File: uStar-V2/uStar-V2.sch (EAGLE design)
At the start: 47 parts, among them IC1 INA138, IC2 SN74HC4066PWRTSSOP, IC3 SN74HC4066PWRTSSOP, IC4 SN74HC4066PWRTSSOP, IC5 SN74HC4066PWRTSSOP, M1 Mount, M2 Mount, U2 SD_CARD, X2 BU-SMA-H, X3 BU-SMA-H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

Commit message: added the 3D parts to the library added cost and hours to the BOM
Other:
- note added: "Feed 5V to pin Vin/Gnd on PWR2"
- note added: "Ground Station Assembly Variant"
- note added: "Jumper BoardVCC to Radio_VCC_3_3"
- note added: "Jumper IC2 and IC4 straight through"
- note added: "Jumper for ground station variant only"

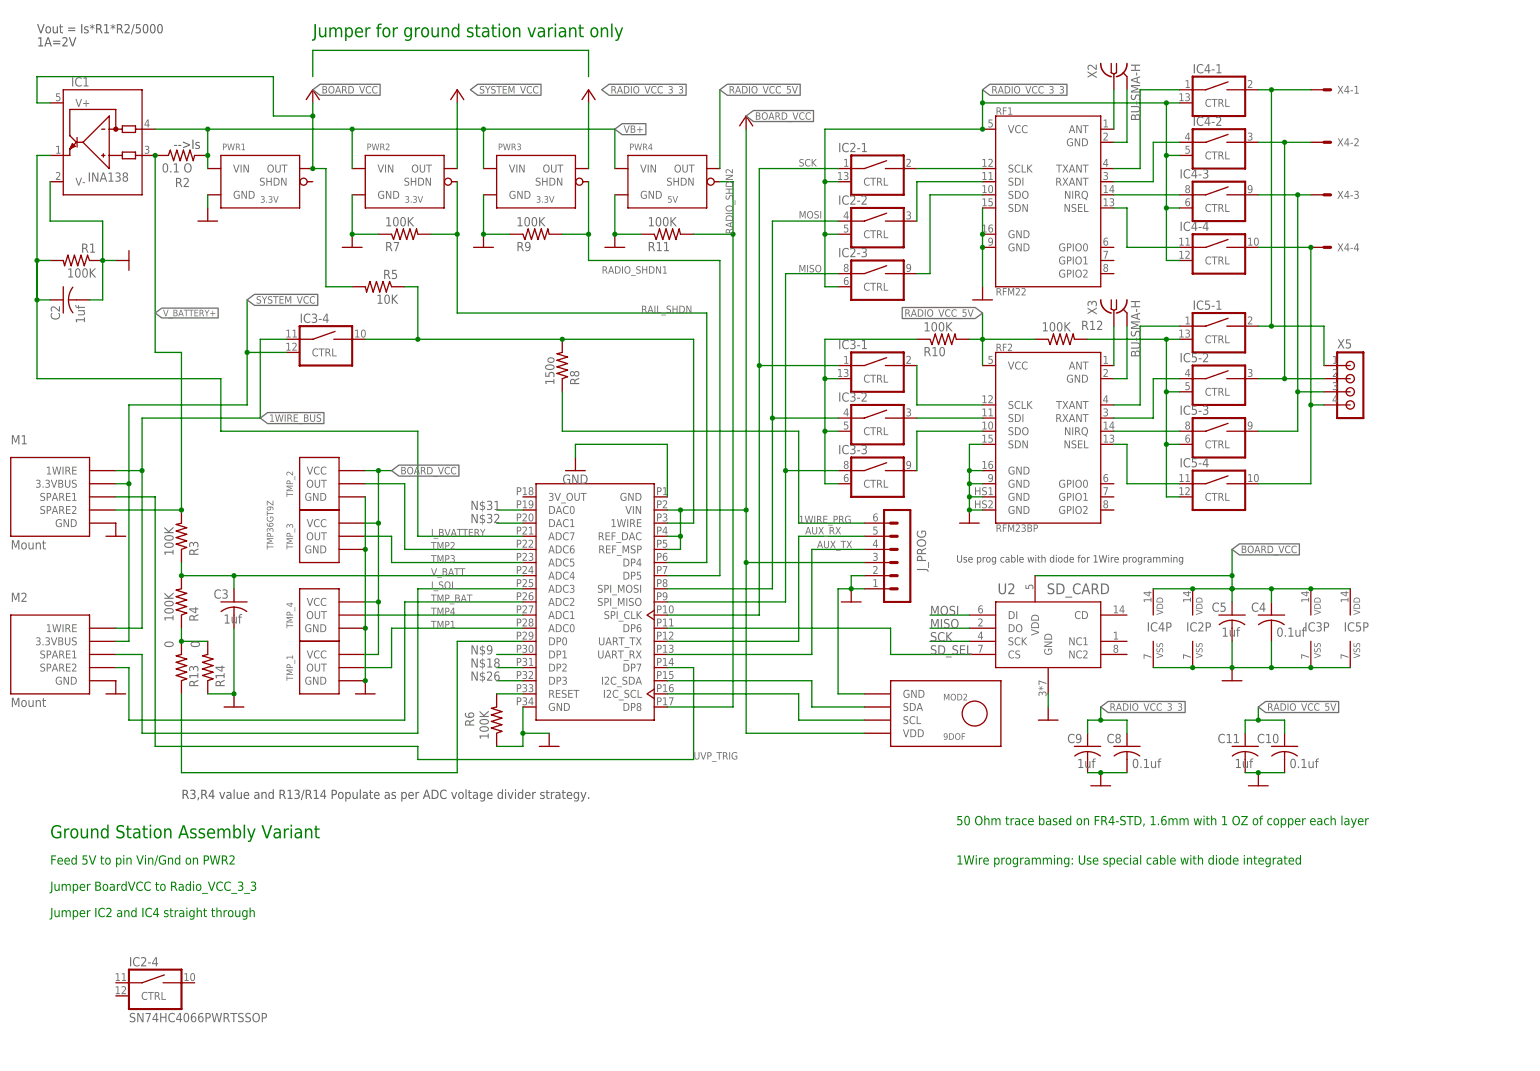
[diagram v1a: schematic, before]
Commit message: 
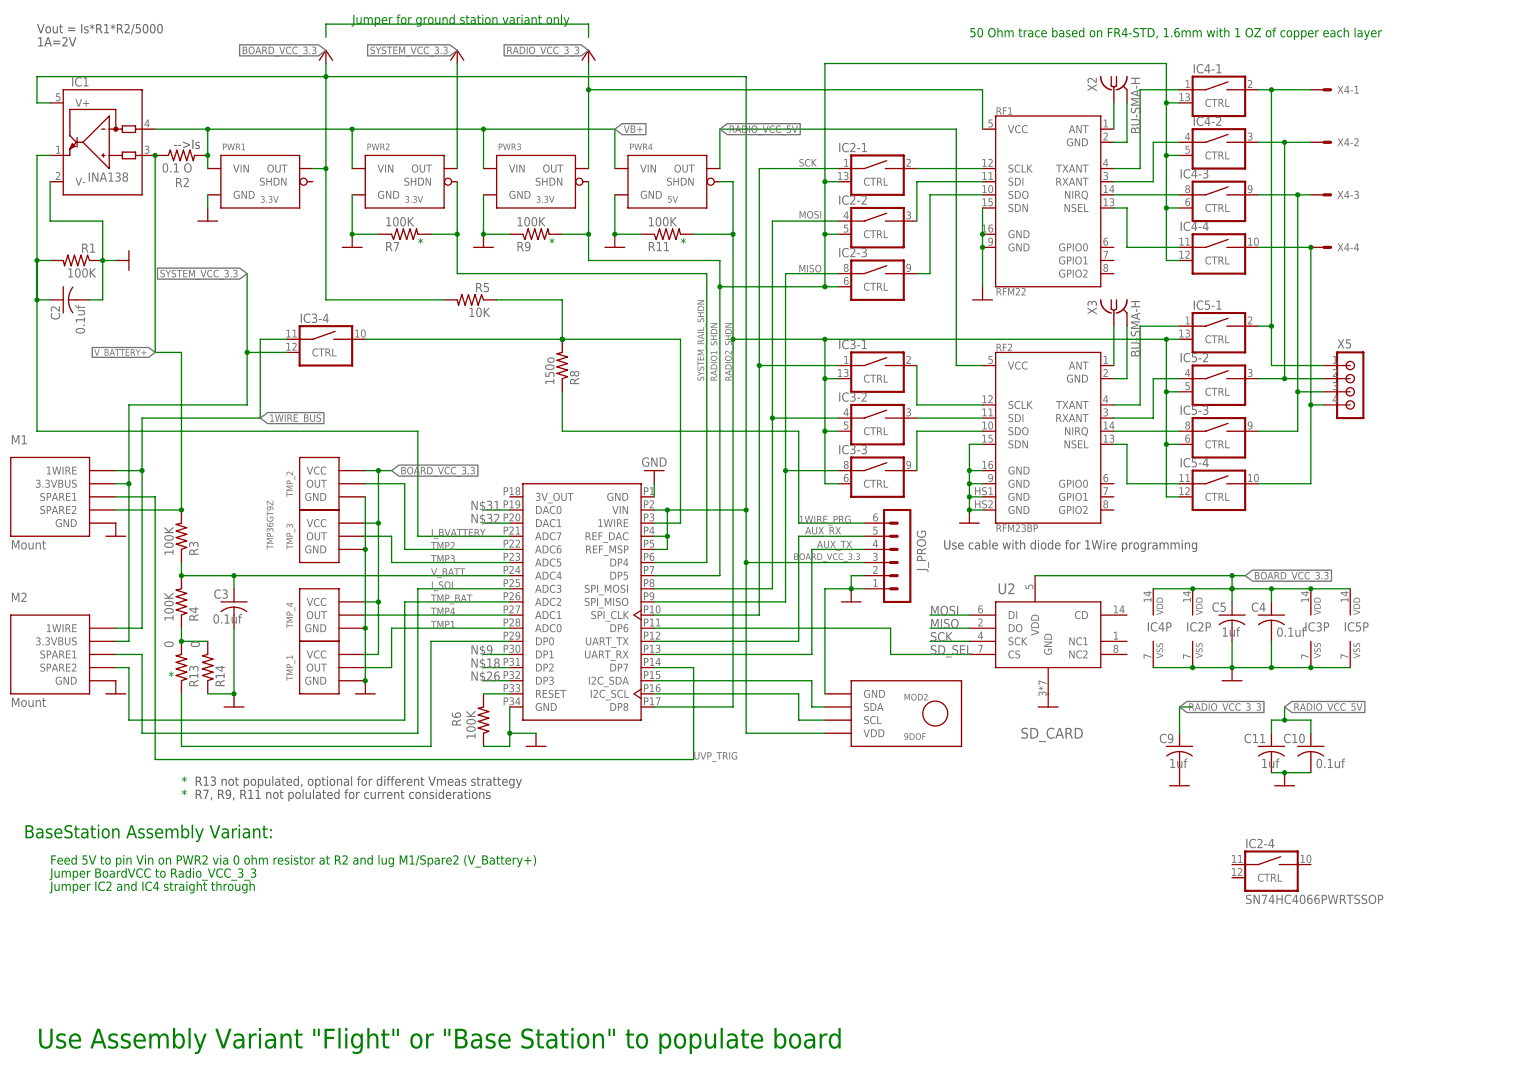
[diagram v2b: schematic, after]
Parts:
- removed C8: 0.1uf, rcl:C-USC0805
- removed R10, R12: 100K, rcl:R-US_R0805
- C2, C3: value 1uf -> 0.1uf
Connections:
- net BOARD_VCC renamed BOARD_VCC_3.3
- net RAIL_SHDN renamed SYSTEM_RAIL_SHDN
- net SYSTEM_VCC renamed SYSTEM_VCC_3.3
- removed net N$4: IC3-1.CTRL, IC3-2.CTRL, IC3-3.CTRL, R10.1
- removed net N$8: IC5-1.CTRL, IC5-2.CTRL, IC5-3.CTRL, IC5-4.CTRL, R12.2
- removed net RADIO_SHDN1: MOD1.DP5, PWR3.SHDN, R9.2
- removed net RADIO_SHDN2: MOD1.DP8, PWR4.SHDN, R11.2
- new net RADIO1_SHDN: IC2-1.CTRL, IC2-2.CTRL, IC2-3.CTRL, IC4-1.CTRL, IC4-2.CTRL, IC4-3.CTRL, IC4-4.CTRL, MOD1.DP5, PWR3.SHDN, R9.2
- new net RADIO2_SHDN: IC3-1.CTRL, IC3-2.CTRL, IC3-3.CTRL, IC5-1.CTRL, IC5-2.CTRL, IC5-3.CTRL, IC5-4.CTRL, MOD1.DP8, PWR4.SHDN, R11.2
- net GND: no longer C8.2
- net RADIO_VCC_3_3: no longer C8.1, IC2-1.CTRL, IC2-2.CTRL, IC2-3.CTRL, IC4-1.CTRL, IC4-2.CTRL, IC4-3.CTRL, IC4-4.CTRL
- net RADIO_VCC_5V: no longer R10.2, R12.1
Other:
- note added: "*"
- note added: "BaseStation Assembly Variant:"
- note added: "Feed 5V to pin Vin on PWR2 via 0 ohm resistor at R2 and lug M1/Spare2 (V_Battery+)"
- note added: "R13 not populated, optional for different Vmeas strattegy"
- note added: "R7, R9, R11 not polulated for current considerations"
- note added: "Use Assembly Variant "Flight" or "Base Station" to populate board"
- note added: "Use cable with diode for 1Wire programming"
- note removed: "1Wire programming: Use special cable with diode integrated"
- note removed: "Feed 5V to pin Vin/Gnd on PWR2"
- note removed: "Ground Station Assembly Variant"
- note removed: "R3,R4 value and R13/R14 Populate as per ADC voltage divider strategy."
- note removed: "Use prog cable with diode for 1Wire programming"
- moved on the sheet: C10, C11, C9, IC2-4, MOD2, R5, R6, X2

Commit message: Changed solder stop mask to fully cover vias to protect from short with RFM23bp. Changed brd rev label to 2.1b to reflect above. Added R9 and R11 back into the flight build - Inadvertently removed when adding the GND station build option. Added wiring schematic for FTDI cable and connector to sch Added ECO sheet to sch change or R6 to Capacitor 0.1uf -- Reset Issue resolve.
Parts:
- added D1: 1N4148DO35-7, diode:1N4148DO35-7
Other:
- note added: "1 Wire /FTDI programming interface:"
- note added: "12/08/21 Affecting PCB Revision 2.1 and 2.1b,Schematic Revision 2.0"
- note added: "12/13/21 Affecting PCB Revision 2.1 and 2.1b,Schematic Revision 2.0"
- note added: "2/25/21 Affecting all builds with radio RFM23bp"
- note added: "Black,GND"
- note added: "FTDI"
- note added: "For BaseStation Jumper IC2: 1-2,3-4,8-9 and IC4 1-2,3-4,8-9,10-11,"
- note added: "J-prog Pin 3 (+3.3V)"
- note added: "J-prog Pin 6 (1 Wire Prog)"
- note added: "J-prog Pin1 (GND)"
- note added: "Jumper for base station variant only"
- note added: "List of Engineering Change Orders (ECO)"
- note added: "Orange, FTDI TX"
- note added: "Place a layer of Kapton tape underneath the big radio where the heatsink pad is located to guard against an eventual short circuit to underlaying traces. V2.1b artwork has covered vias and tape is merely a safety precautoion."
- note added: "R6 : Remove and replace with 805/ 0.1uF ceramic capacitor. Guards against a inadvertant reset condition in an noisy EMF enwironment"
- note added: "R6 changed to 0.1uF capacitor instead of 100k resistor"
- note added: "R7 not polulated for current considerations"
- note added: "R9, R11: Add 805/R10K resistor on empty pads for R9 , R11. Affects the startup sequence of radio power and prevents potential sporadic transmission during uP bootup sequence."
- note added: "Red +3.3V"
- note added: "Yellow, FTDI RX"
- note removed: "Jumper for ground station variant only"
- note removed: "R7, R9, R11 not polulated for current considerations"
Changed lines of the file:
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@@
 <layer number="59" name="tCarbon" color="7" fill="1" visible="no" active="no"/>
 <layer number="60" name="bCarbon" color="7" fill="1" visible="no" active="no"/>
-<layer number="88" name="SimResults" color="9" fill="1" visible="no" active="yes"/>
+<layer number="88" name="SimResults" color="9" fill="1" visible="yes" active="yes"/>
 <layer number="89" name="SimProbes" color="9" fill="1" visible="no" active="yes"/>
 <layer number="90" name="Modules" color="5" fill="1" visible="no" active="yes"/>
@@
 <variantdefs>
 <variantdef name="BaseSation"/>
-<variantdef name="Flight"/>
+<variantdef name="Flight" current="yes"/>
 </variantdefs>
 <classes>
@@
 <attribute name="DIGIKEY" value="2019-RK73H2ATTD1003FCT-ND"/>
 <variant name="BaseSation" populate="no"/>
-<variant name="Flight" populate="no"/>
 </part>
 <part name="R6" library="rcl" library_urn="urn:adsk.eagle:library:334" deviceset="R-US_" device="R0805" package3d_urn="urn:adsk.eagle:package:23553/2" value="100K">
 <attribute name="DIGIKEY" value="2019-RK73H2ATTD1003FCT-ND"/>
+<variant name="BaseSation" populate="no"/>
+<variant name="Flight" populate="no"/>
 </part>
 <part name="X4" library="newUstar" deviceset="?M04B-SRSS-TB" device="S" package3d_urn="urn:adsk.eagle:package:25263025/2">
@@
 <attribute name="DIGIKEY" value="2019-RK73H2ATTD1003FCT-ND"/>
 <variant name="BaseSation" populate="no"/>
-<variant name="Flight" populate="no"/>
 </part>
 <part name="IC4" library="newUstar" deviceset="SN74HC4066PWR" device="TSSOP" package3d_urn="urn:adsk.eagle:package:25264417/2">
@@
 <variant name="BaseSation" populate="no"/>
 </part>
+<part name="D1" library="diode" library_urn="urn:adsk.eagle:library:210" deviceset="1N4148" device="DO35-7" package3d_urn="urn:adsk.eagle:package:43339/2"/>
 </parts>
 <sheets>
@@
 <text x="-93.98" y="78.74" size="1.778" layer="91">Jumper IC2 and IC4 straight through</text>
 <text x="-93.98" y="83.82" size="1.778" layer="91">Feed 5V to pin Vin on PWR2 via 0 ohm resistor at R2 and lug M1/Spare2 (V_Battery+)</text>
-<text x="-99.06" y="88.9" size="2.54" layer="91">BaseStation Assembly Variant:</text>
-<text x="-35.56" y="246.38" size="1.778" layer="91">Jumper for ground station variant only</text>
+<text x="-93.98" y="88.9" size="2.54" layer="91">BaseStation Assembly Variant:</text>
+<text x="-35.56" y="246.38" size="1.778" layer="97">Jumper for base station variant only</text>
 <text x="-71.12" y="119.38" size="1.778" layer="91">*</text>
 <text x="-68.58" y="99.06" size="1.778" layer="91">*</text>
@@
 <text x="27.94" y="203.2" size="1.778" layer="91">*</text>
 <text x="-68.58" y="96.52" size="1.778" layer="91">*</text>
-<text x="-66.04" y="96.52" size="1.778" layer="97">R7, R9, R11 not polulated for current considerations</text>
+<text x="-66.04" y="96.52" size="1.778" layer="97">R7 not polulated for current considerations</text>
+<text x="84.328" y="240.03" size="1.778" layer="97">For BaseStation  Jumper IC2: 1-2,3-4,8-9 and IC4 1-2,3-4,8-9,10-11,</text>
+<text x="-91.44" y="71.12" size="2.54" layer="96">1 Wire /FTDI  programming interface:</text>
+<wire x1="-76.2" y1="68.58" x2="-38.1" y2="68.58" width="0.1524" layer="96"/>
+<wire x1="-78.74" y1="66.04" x2="-43.18" y2="66.04" width="0.1524" layer="96"/>
+<wire x1="-43.18" y1="66.04" x2="-38.1" y2="66.04" width="0.1524" layer="96"/>
+<wire x1="-76.2" y1="63.5" x2="-50.8" y2="63.5" width="0.1524" layer="96"/>
+<wire x1="-76.2" y1="60.96" x2="-38.1" y2="60.96" width="0.1524" layer="96"/>
+<polygon width="0.1524" layer="96">
+<vertex x="-91.44" y="68.58"/>
+<vertex x="-76.2" y="68.58"/>
+<vertex x="-76.2" y="60.96"/>
+<vertex x="-91.44" y="60.96"/>
+</polygon>
+<polygon width="0.1524" layer="96">
+<vertex x="-91.694" y="67.564"/>
+<vertex x="-91.694" y="61.976"/>
+<vertex x="-97.536" y="61.976"/>
+<vertex x="-97.536" y="67.564"/>
+</polygon>
+<text x="-88.9" y="63.5" size="2.54" layer="88">FTDI</text>
+<text x="-71.12" y="68.834" size="1.016" layer="94">Red +3.3V</text>
+<text x="-71.12" y="66.548" size="1.016" layer="94">Yellow, FTDI RX</text>
+<text x="-71.374" y="64.008" size="1.016" layer="94">Orange, FTDI TX</text>
+<text x="-71.374" y="61.468" size="1.016" layer="94">Black,GND</text>
+<wire x1="-45.72" y1="63.5" x2="-43.18" y2="63.5" width="0.1524" layer="96"/>
+<text x="-35.56" y="60.96" size="1.27" layer="96">J-prog Pin1 (GND)</text>
+<wire x1="-43.18" y1="63.5" x2="-43.18" y2="66.04" width="0.1524" layer="96"/>
+<text x="-35.56" y="66.04" size="1.27" layer="96">J-prog Pin 6 (1 Wire Prog)</text>
+<text x="-35.56" y="68.58" size="1.27" layer="96">J-prog Pin 3 (+3.3V)</text>
+<text x="-66.04" y="93.98" size="1.778" layer="97">R6 changed to 0.1uF capacitor instead of 100k resistor</text>
 </plain>
 <instances>
@@
 <attribute name="NAME" x="-45.72" y="188.595" size="1.778" layer="95"/>
 </instance>
-<instance part="IC2" gate="-4" x="142.24" y="81.28" smashed="yes">
-<attribute name="NAME" x="137.16" y="86.995" size="1.778" layer="95"/>
-<attribute name="VALUE" x="137.16" y="76.2" size="1.778" layer="96"/>
+<instance part="IC2" gate="-4" x="137.16" y="81.28" smashed="yes">
+<attribute name="NAME" x="132.08" y="86.995" size="1.778" layer="95"/>
+<attribute name="VALUE" x="132.08" y="76.2" size="1.778" layer="96"/>
 </instance>
 <instance part="IC5" gate="P" x="157.48" y="129.54" smashed="yes">
@@
 <attribute name="DIGIKEY" x="-63.5" y="121.92" size="1.778" layer="96" rot="MR90" display="off"/>
 </instance>
+<instance part="D1" gate="G$1" x="-48.26" y="63.5" smashed="yes" rot="R180"/>
 </instances>
 <busses>
@@
 </nets>
 </sheet>
+<sheet>
+<plain>
+<text x="-22.86" y="147.32" size="3.81" layer="94">List of Engineering Change Orders (ECO)</text>
+<text x="-22.86" y="119.888" size="1.778" layer="91">12/13/21 Affecting PCB Revision 2.1 and 2.1b,Schematic Revision 2.0</text>
+<text x="-22.86" y="116.84" size="1.016" layer="91">R6 : Remove and replace with 805/ 0.1uF ceramic capacitor.
+Guards against a inadvertant reset condition in an noisy EMF enwironment</text>
+<text x="-22.86" y="132.842" size="1.778" layer="91">12/08/21 Affecting PCB Revision 2.1 and 2.1b,Schematic Revision 2.0</text>
+<text x="-22.86" y="129.54" size="1.016" layer="91">R9, R11: Add 805/R10K resistor on empty pads for R9 , R11.
+  Affects the startup sequence of radio power and prevents potential sporadic transmission during uP bootup sequence.</text>
+<text x="-22.86" y="143.002" size="1.778" layer="91">2/25/21 Affecting all builds with radio RFM23bp</text>
+<text x="-22.86" y="139.7" size="1.016" layer="91">Place a layer of Kapton tape underneath the big radio where the heatsink pad is located to guard against an eventual short circuit to underlaying traces.
+ V2.1b artwork has covered vias and tape is merely a safety precautoion. </text>
+</plain>
+<instances>
+</instances>
+<busses>
+</busses>
+<nets>
+</nets>
+</sheet>
 </sheets>
 </schematic>
 </drawing>
 <compatibility>
+<note version="6.3" minversion="6.2.2" severity="warning">
+Since Version 6.2.2 text objects can contain more than one line,
+which will not be processed correctly with this version.
+</note>
 <note version="8.2" severity="warning">
 Since Version 8.2, EAGLE supports online libraries. The ids
